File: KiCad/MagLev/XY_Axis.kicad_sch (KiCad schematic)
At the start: 26 parts, among them Q1 ZX5T851GTA, Q2 ZX5T1951GTA, Q3 ZX5T851GTA, Q4 ZX5T1951GTA, U1 LM324

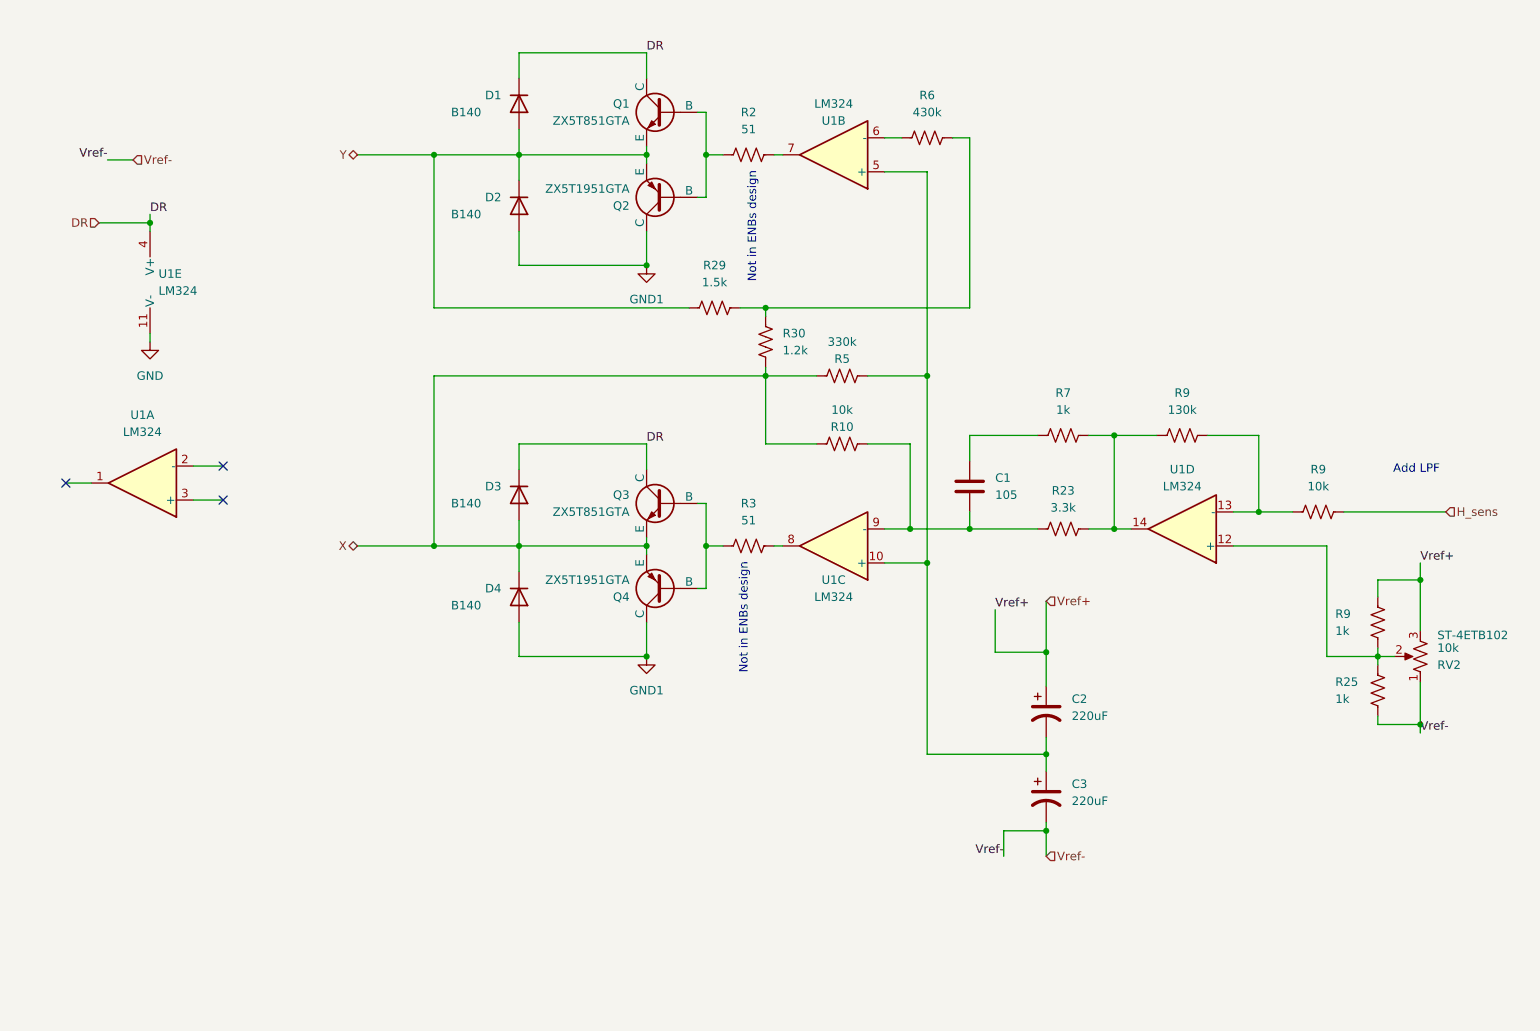
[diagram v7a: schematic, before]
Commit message: Add MCU enable circuit and leds.
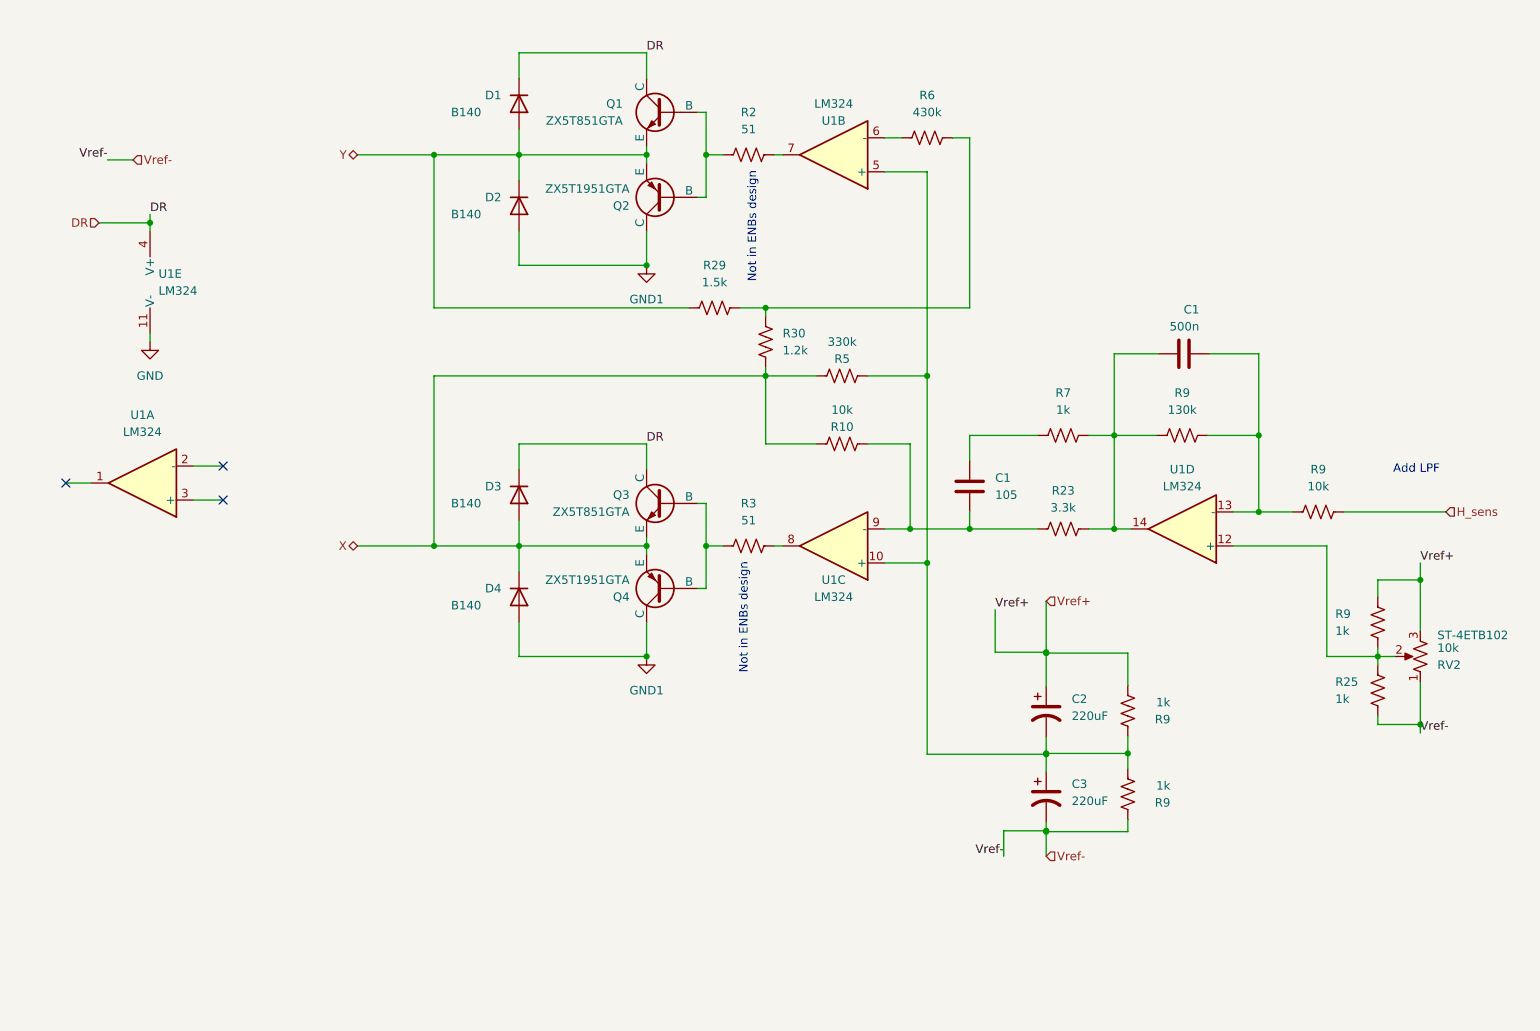
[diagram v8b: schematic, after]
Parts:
- added C1: 500n, Capacitor_SMD:C_0805_2012Metric_Pad1.18x1.45mm_HandSolder, symbol Device:C
- added R9 (x2): 1k, Resistor_SMD:R_0805_2012Metric_Pad1.20x1.40mm_HandSolder, symbol Device:R_US
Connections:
- net Vref+: now also R9.1
- net Vref-: now also R9.2
- net at R9.1, R9.2, U1.13 (-): now also C1.2
- net at R23.2, R7.2, R9.1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: now also C1.1
- net at C2.2, C3.1, R5.1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: now also R9.1, R9.2
